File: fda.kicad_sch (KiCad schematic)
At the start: 43 parts, among them U706 OPA2197D, U73 OPA2388DGK, U74 THS4521IDGK

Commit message: Progress checkin.  About to redo FDA feedback again.
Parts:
- renumbered C70 to C72
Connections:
- net +5VA: now also R728.1; no longer R728.2
- net IN-: now also R735.1; no longer R735.2
- net In+Fb-: now also C724.2; no longer C724.1
- net Out+: now also R737.1, R738.1; no longer R737.2, R738.2
- net S2Bias: now also R728.2; no longer R728.1
- net at C730.2, R736.2, U706.7: now also R737.2, R738.2; no longer R737.1, R738.1
- net at R740.2: now also C724.1; no longer C724.2
- net at C730.1, R736.1, U706.6 (-): now also R735.2; no longer R735.1
- net -18V renamed -16V
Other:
- moved on the sheet: C724, R737, R738
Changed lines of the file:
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@@
 		(lib_id "Device:R")
 		(at 128.27 118.11 270)
-		(mirror x)
 		(unit 1)
 		(exclude_from_sim no)
@@
 		)
 		(property "Footprint" "Resistor_SMD:R_0402_1005Metric"
-			(at 128.27 119.888 90)
+			(at 128.27 116.332 90)
 			(effects
 				(font
@@
 		(lib_id "Device:R")
 		(at 128.27 90.17 270)
-		(mirror x)
 		(unit 1)
 		(exclude_from_sim no)
@@
 		)
 		(property "Footprint" "Resistor_SMD:R_0402_1005Metric"
-			(at 128.27 91.948 90)
+			(at 128.27 88.392 90)
 			(effects
 				(font
@@
 		(lib_id "Device:R")
 		(at 109.22 99.06 270)
-		(mirror x)
 		(unit 1)
 		(exclude_from_sim no)
@@
 		)
 		(property "Footprint" "Resistor_SMD:R_0402_1005Metric"
-			(at 109.22 100.838 90)
+			(at 109.22 97.282 90)
 			(effects
 				(font
@@
 		(lib_id "Device:C")
 		(at 143.51 99.06 0)
-		(mirror y)
 		(unit 1)
 		(exclude_from_sim no)
@@
 					(size 1.27 1.27)
 				)
-				(justify left)
+				(justify right)
 			)
 		)
@@
 					(size 1.27 1.27)
 				)
-				(justify left)
+				(justify right)
 			)
 		)
 		(property "Footprint" "Capacitor_SMD:C_0603_1608Metric"
-			(at 142.5448 102.87 0)
+			(at 144.4752 102.87 0)
 			(effects
 				(font
@@
 		(lib_id "Device:R")
 		(at 96.52 104.14 0)
-		(mirror x)
 		(unit 1)
 		(exclude_from_sim no)
@@
 	(symbol
 		(lib_id "Device:R")
-		(at 91.44 146.05 180)
+		(at 91.44 146.05 0)
 		(unit 1)
 		(exclude_from_sim no)
@@
 		)
 		(property "Footprint" "Resistor_SMD:R_0402_1005Metric"
-			(at 93.218 146.05 90)
+			(at 89.662 146.05 90)
 			(effects
 				(font
@@
 		(on_board yes)
 		(dnp no)
-		(property "Reference" "C70"
+		(property "Reference" "C72"
 			(at 104.14 154.432 0)
 			(effects
@@
 			(project "lincal"
 				(path "/b054cef4-39e3-49d8-aff0-7ba5a206c187/91ba7742-b0d4-4498-bde0-79d5f38f349f"
-					(reference "C70")
+					(reference "C72")
 					(unit 1)
 				)
@@
 	(symbol
 		(lib_id "Device:R")
-		(at 93.98 146.05 180)
+		(at 93.98 146.05 0)
 		(unit 1)
 		(exclude_from_sim no)
@@
 		(dnp no)
 		(property "Reference" "R738"
-			(at 96.266 146.05 90)
+			(at 96.012 146.05 90)
 			(effects
 				(font
@@
 		)
 		(property "Footprint" "Resistor_SMD:R_0603_1608Metric"
-			(at 95.758 146.05 90)
+			(at 92.202 146.05 90)
 			(effects
 				(font
@@
 		(dnp no)
 		(property "Reference" "R733"
-			(at 89.154 62.23 90)
+			(at 89.408 62.23 90)
 			(effects
 				(font
@@
 	(symbol
 		(lib_id "Device:C")
-		(at 96.52 86.36 180)
+		(at 96.52 86.36 0)
 		(unit 1)
 		(exclude_from_sim no)
@@
 		(dnp no)
 		(property "Reference" "C724"
-			(at 96.52 84.328 0)
+			(at 96.52 88.392 0)
 			(effects
 				(font
 					(size 1.27 1.27)
 				)
-				(justify right)
+				(justify left)
 			)
 		)
 		(property "Value" "330p"
-			(at 96.52 88.646 0)
+			(at 96.52 84.074 0)
 			(effects
 				(font
 					(size 1.27 1.27)
 				)
-				(justify right)
+				(justify left)
 			)
 		)
 		(property "Footprint" "Capacitor_SMD:C_0603_1608Metric"
-			(at 95.5548 82.55 0)
+			(at 97.4852 90.17 0)
 			(effects
 				(font
@@
 		(lib_id "Device:R")
 		(at 93.98 62.23 0)
-		(mirror y)
 		(unit 1)
 		(exclude_from_sim no)
@@
 		(dnp no)
 		(property "Reference" "R734"
-			(at 96.266 62.23 90)
+			(at 96.012 62.23 90)
 			(effects
 				(font
@@
 		)
 		(property "Footprint" "Resistor_SMD:R_0603_1608Metric"
-			(at 95.758 62.23 90)
+			(at 92.202 62.23 90)
 			(effects
 				(font
@@
 	)
 	(symbol
-		(lib_id "Parts:-18V")
+		(lib_id "Parts:-16V")
 		(at 181.61 81.28 0)
 		(unit 1)
@@
 		(on_board yes)
 		(dnp no)
-		(property "Reference" "#PWR0149"
+		(property "Reference" "#PWR149"
 			(at 181.61 77.47 0)
 			(effects
@@
 			)
 		)
-		(property "Value" "-18V"
+		(property "Value" "-16V"
 			(at 181.61 84.836 0)
 			(do_not_autoplace yes)
@@
 			)
 		)
-		(property "Description" "Power symbol creates a global label with name \"-18V\""
+		(property "Description" "Power symbol creates a global label with name \"-16V\""
 			(at 181.61 81.28 0)
 			(effects
@@
 			(project "lincal"
 				(path "/b054cef4-39e3-49d8-aff0-7ba5a206c187/91ba7742-b0d4-4498-bde0-79d5f38f349f"
-					(reference "#PWR0149")
+					(reference "#PWR149")
 					(unit 1)
 				)
@@
 		(lib_id "Device:R")
 		(at 69.85 135.89 0)
-		(mirror x)
 		(unit 1)
 		(exclude_from_sim no)

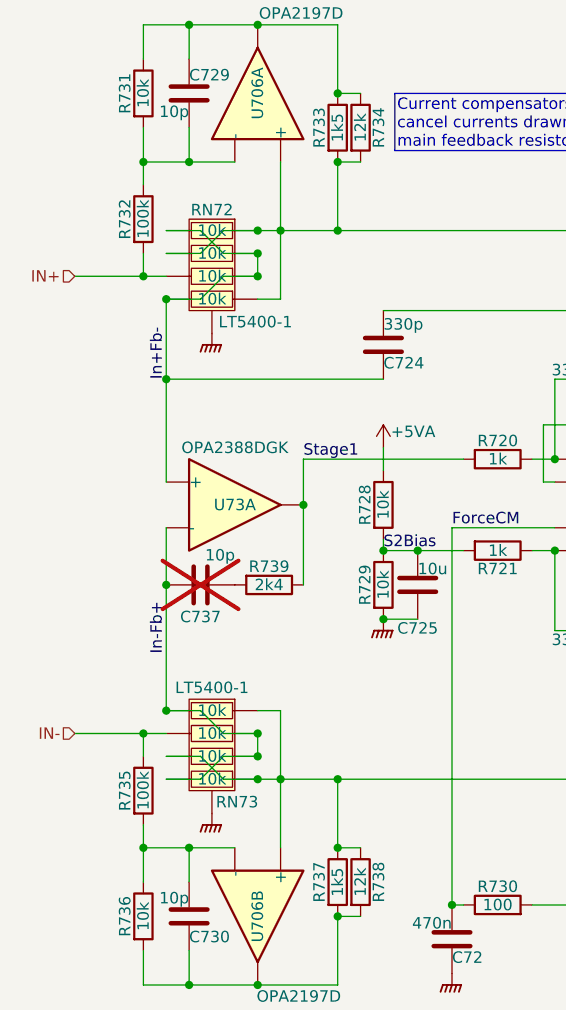
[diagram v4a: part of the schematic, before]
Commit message: Start to place within physical board size.
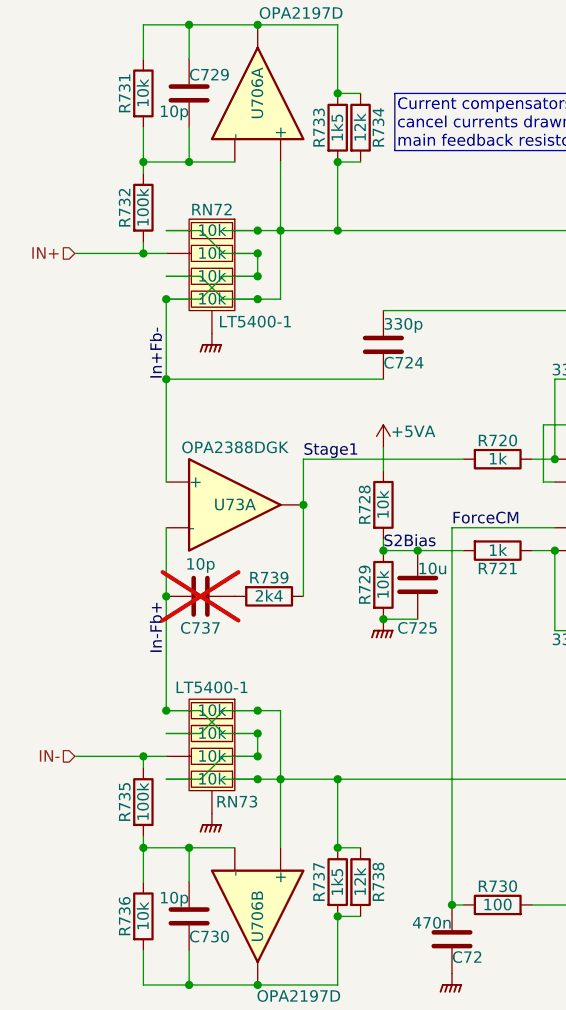
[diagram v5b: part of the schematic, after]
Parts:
- R733, R737: footprint Resistor_SMD:R_0402_1005Metric -> Resistor_SMD:R_0603_1608Metric; LCSC C25867 -> (none)
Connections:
- net IN+: now also RN72.7; no longer RN72.6
- net IN-: now also RN73.6; no longer RN73.7
- net Out+: now also RN73.7; no longer RN73.6
- net Out-: now also RN72.6; no longer RN72.7
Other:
- moved on the sheet: C737, R732, R735, R739

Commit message: Adjust placements
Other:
- moved on the sheet: R730
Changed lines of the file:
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@@
 	(wire
 		(pts
-			(xy 113.03 148.59) (xy 118.11 148.59)
+			(xy 115.57 148.59) (xy 118.11 148.59)
 		)
 		(stroke
@@
 	(wire
 		(pts
-			(xy 104.14 148.59) (xy 105.41 148.59)
+			(xy 104.14 148.59) (xy 107.95 148.59)
 		)
 		(stroke
@@
 		(effects
 			(font
-				(size 1.27 1.27)
+				(size 1.016 1.016)
 			)
 			(justify left bottom)
@@
 		(effects
 			(font
-				(size 1.27 1.27)
+				(size 1.016 1.016)
 			)
 			(justify left bottom)
@@
 		(effects
 			(font
-				(size 1.27 1.27)
+				(size 1.016 1.016)
 			)
 			(justify left bottom)
@@
 		(effects
 			(font
-				(size 1.27 1.27)
+				(size 1.016 1.016)
 			)
 			(justify left bottom)
@@
 		(effects
 			(font
-				(size 1.27 1.27)
+				(size 1.016 1.016)
 			)
 			(justify left bottom)
@@
 	(symbol
 		(lib_id "Device:R")
-		(at 109.22 148.59 90)
+		(at 111.76 148.59 90)
 		(unit 1)
 		(exclude_from_sim no)
@@
 		(dnp no)
 		(property "Reference" "R730"
-			(at 109.22 146.558 90)
+			(at 111.76 146.558 90)
 			(effects
 				(font
@@
 		)
 		(property "Value" "100"
-			(at 109.22 148.59 90)
+			(at 111.76 148.59 90)
 			(effects
 				(font
@@
 		)
 		(property "Footprint" "Resistor_SMD:R_0402_1005Metric"
-			(at 109.22 150.368 90)
+			(at 111.76 150.368 90)
 			(effects
 				(font
@@
 		)
 		(property "Datasheet" "~"
-			(at 109.22 148.59 0)
+			(at 111.76 148.59 0)
 			(effects
 				(font
@@
 		)
 		(property "Description" "Resistor"
-			(at 109.22 148.59 0)
+			(at 111.76 148.59 0)
 			(effects
 				(font
@@
 		)
 		(property "LCSC" "C25076"
-			(at 109.22 148.59 90)
+			(at 111.76 148.59 90)
 			(effects
 				(font
@@
 		)
 		(property "Stock" ""
-			(at 109.22 148.59 90)
+			(at 111.76 148.59 90)
 			(effects
 				(font

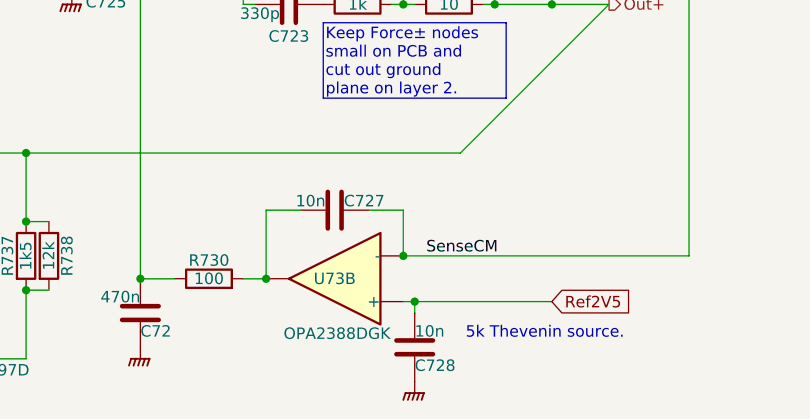
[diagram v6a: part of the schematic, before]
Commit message: Power mostly routed
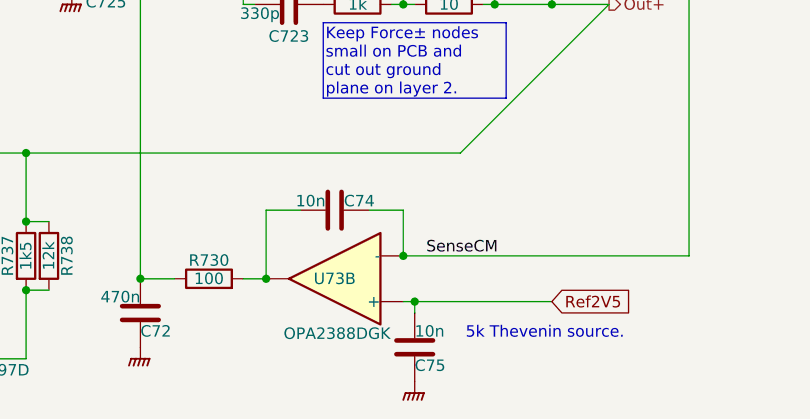
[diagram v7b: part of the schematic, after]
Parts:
- renumbered C727 to C74, C728 to C75
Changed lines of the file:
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@@
 		(on_board yes)
 		(dnp no)
-		(property "Reference" "C728"
+		(property "Reference" "C75"
 			(at 134.62 158.242 0)
 			(effects
@@
 			(project "lincal"
 				(path "/b054cef4-39e3-49d8-aff0-7ba5a206c187/91ba7742-b0d4-4498-bde0-79d5f38f349f"
-					(reference "C728")
+					(reference "C75")
 					(unit 1)
 				)
@@
 		(on_board yes)
 		(dnp no)
-		(property "Reference" "C727"
+		(property "Reference" "C74"
 			(at 126.746 139.954 90)
 			(effects
@@
 			(project "lincal"
 				(path "/b054cef4-39e3-49d8-aff0-7ba5a206c187/91ba7742-b0d4-4498-bde0-79d5f38f349f"
-					(reference "C727")
-					(unit 1)
-				)
+					(reference "C74")
+					(unit 1)
+				)

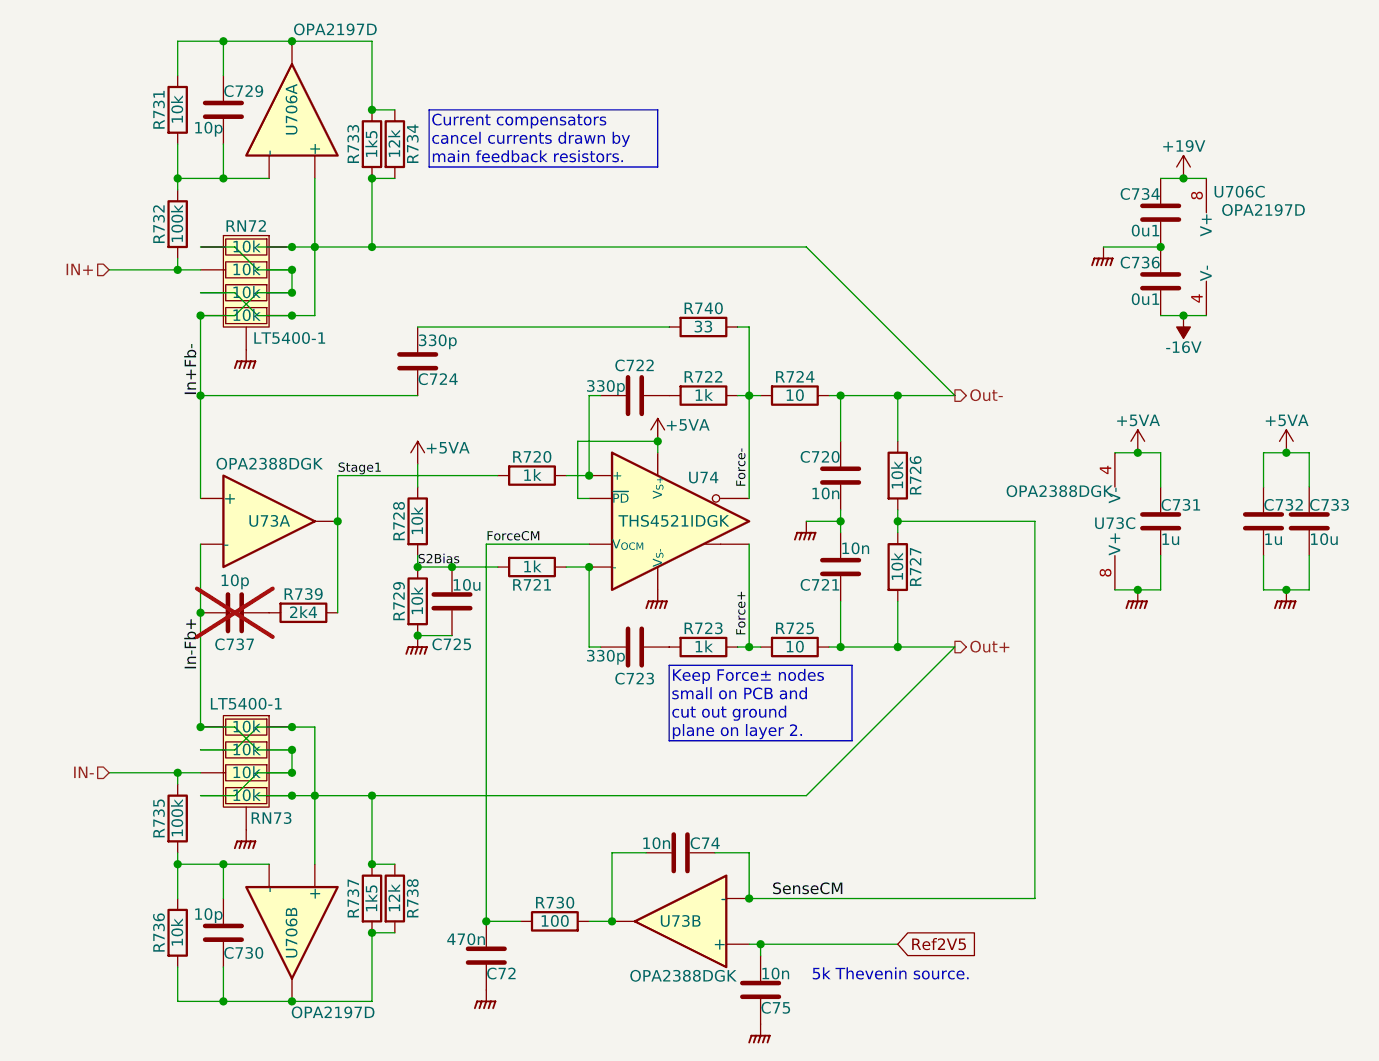
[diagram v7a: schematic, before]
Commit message: Nearly all routed.  Repinning FDA resistors.
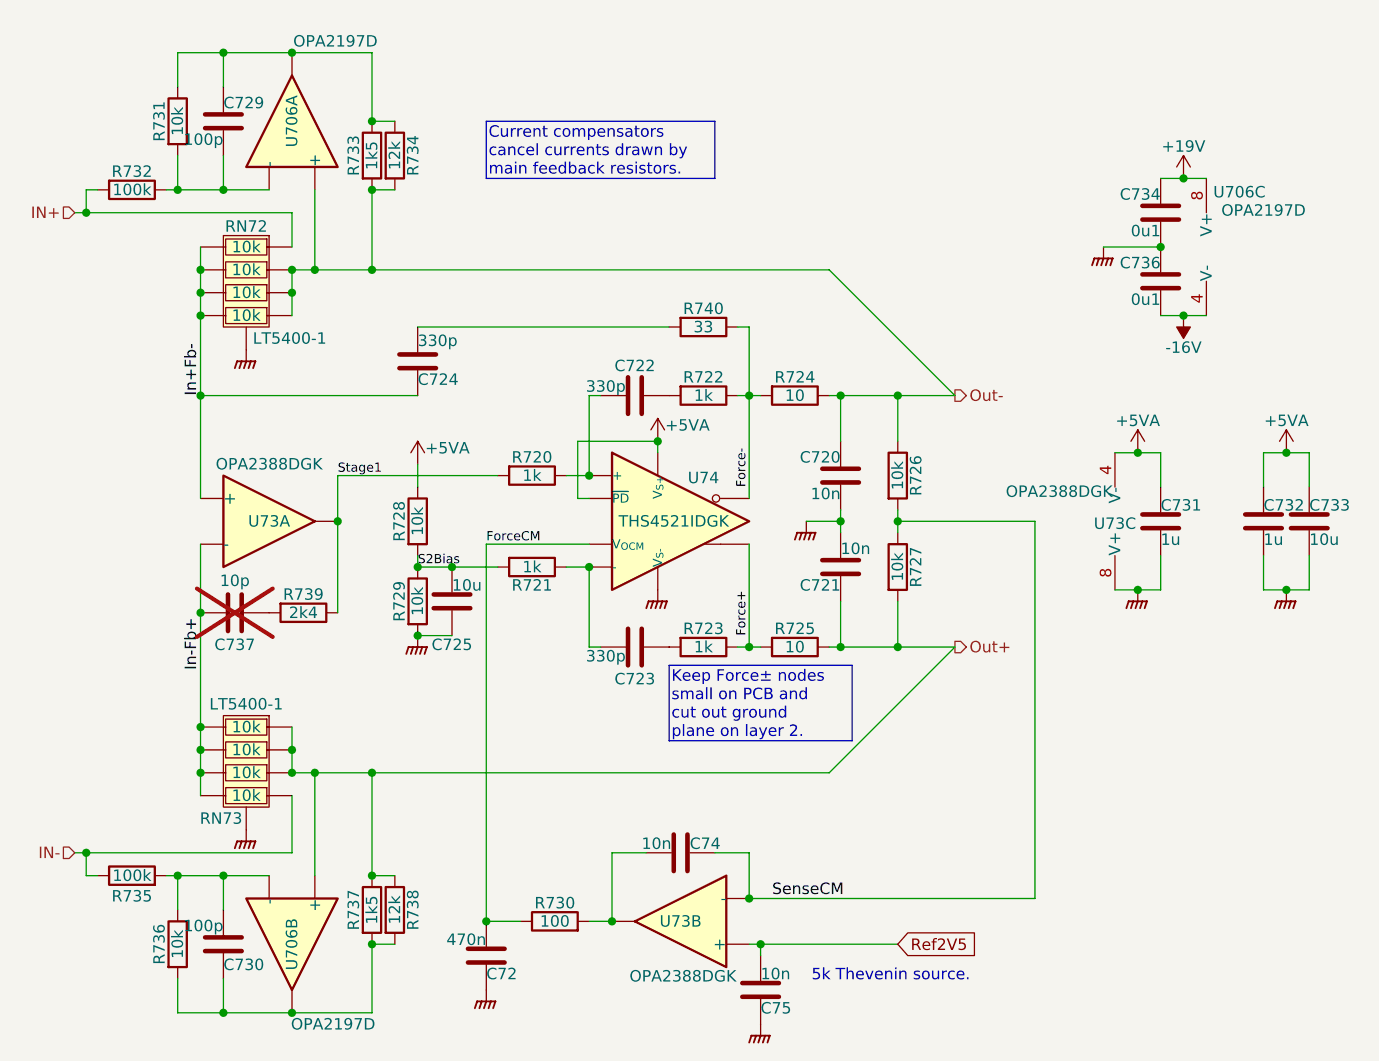
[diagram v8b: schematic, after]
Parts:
- C729, C730: value 10p -> 100p; LCSC C32949 -> (none)
- R740: LCSC (none) -> C25105
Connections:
- net IN+: now also RN72.1; no longer RN72.7
- net IN-: now also RN73.4; no longer RN73.6
- net In+Fb-: now also RN72.6, RN72.7; no longer RN72.2, RN72.3
- net In-Fb+: now also RN73.6, RN73.7; no longer RN73.2, RN73.3
- net Out+: now also RN73.2, RN73.3; no longer RN73.4, RN73.7
- net Out-: now also RN72.2, RN72.3; no longer RN72.1, RN72.6
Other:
- moved on the sheet: C729, C730, R731, R732, R733, R734, R735, R736, R737, R738, U706A, U706B
